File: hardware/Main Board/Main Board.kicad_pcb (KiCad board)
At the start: 2 copper layers, 119 x 56 mm, 32 parts, among them J1 DEC Motor, J2 RA Motor, J3 Battery, J4 Joystick Debug, J5 Joystick Connector, P1 Conn_02x20_Odd_Even, Q1 2N3904, Q2 2N3904, Q3 2N3904, Q4 2N3904, Q5 2N3904, U1 ELEGOO, U2 RA Driver, U3 BuckConverter, U4 BuckConverter

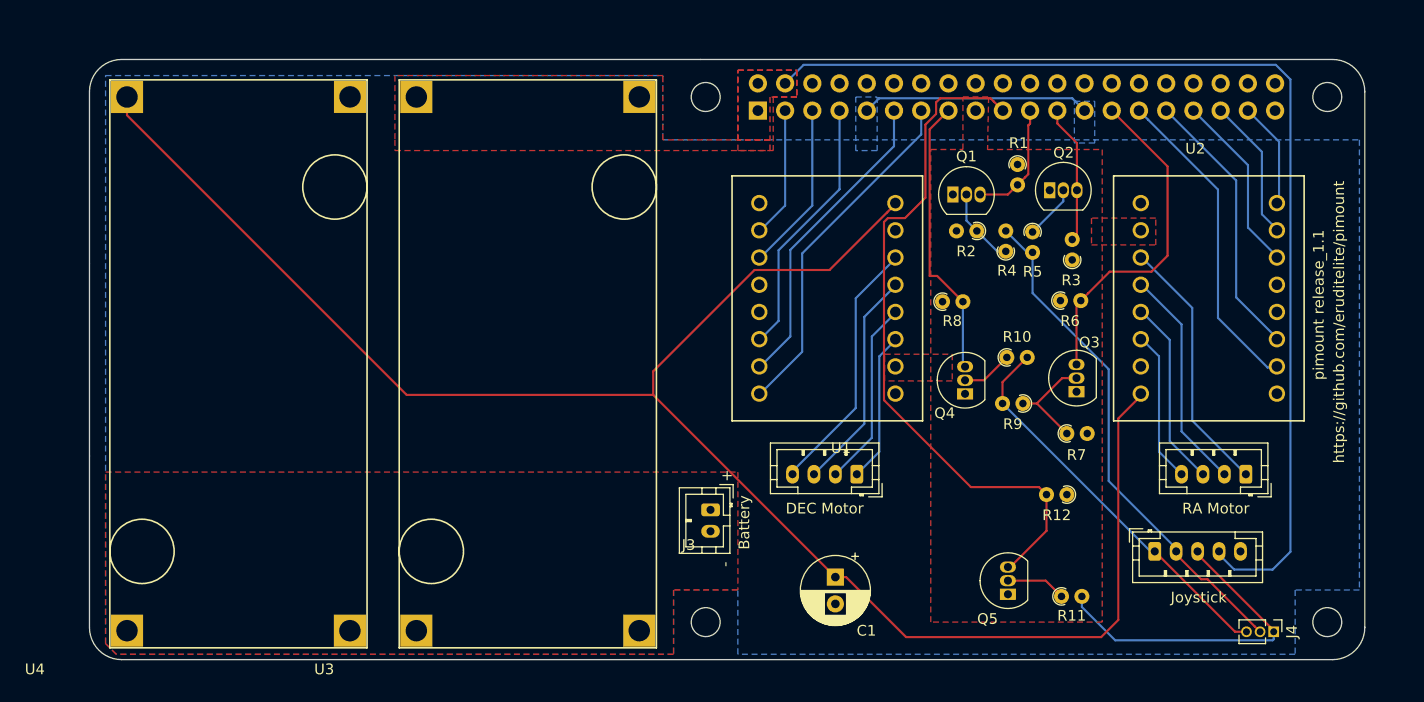
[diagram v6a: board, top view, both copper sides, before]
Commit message: Add a Fan Control Circuit
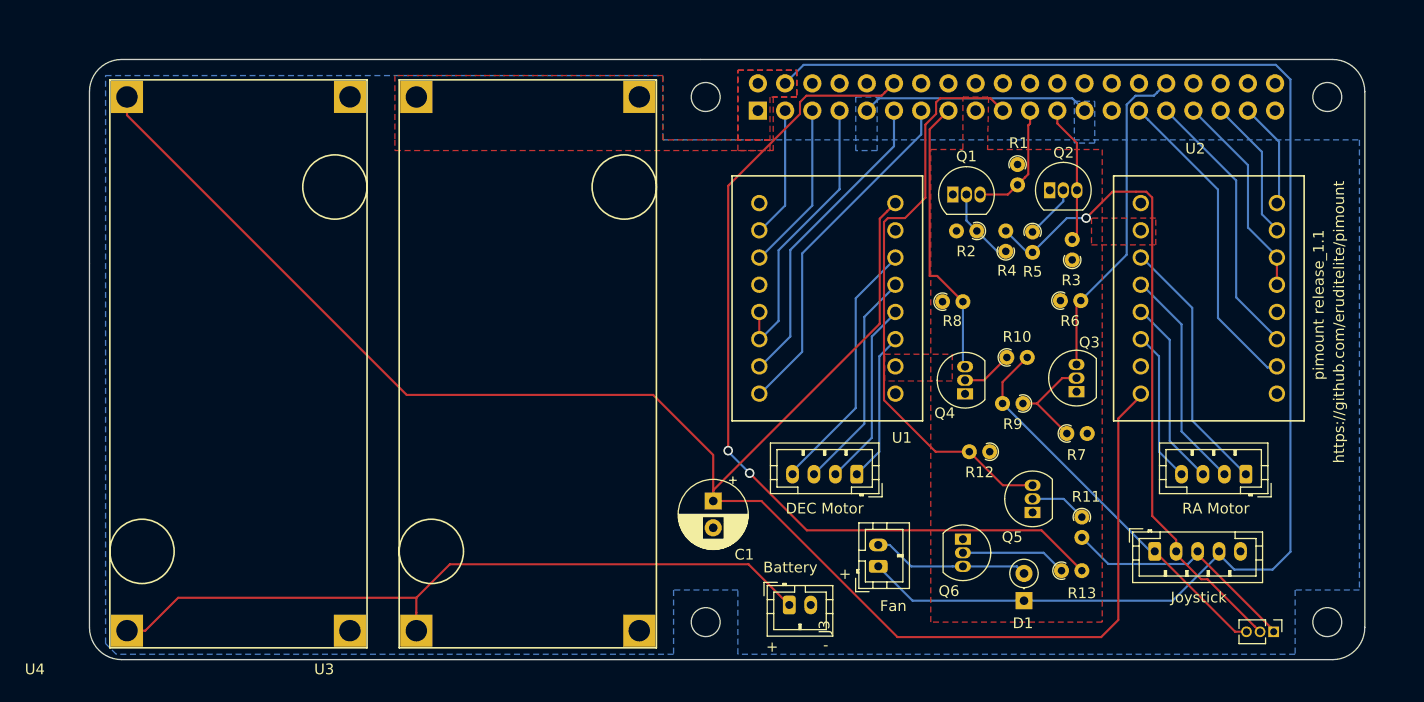
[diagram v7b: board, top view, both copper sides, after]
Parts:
- added D1: 1N4148, Diode_THT:D_DO-35_SOD27_P2.54mm_Vertical_KathodeUp, F.Cu at (229.7, 148.0)
- added J6: Fan, Connector_JST:JST_PH_B2B-PH-K_1x02_P2.00mm_Vertical, F.Cu at (216.1, 144.8)
- added Q6: S8050, Package_TO_SOT_THT:TO-92_Inline, F.Cu at (224.0, 142.3)
- added R13: 1K, Resistor_THT:R_Axial_DIN0204_L3.6mm_D1.6mm_P1.90mm_Vertical, F.Cu at (233.2, 145.2)
- moved C1 13.4 mm to (200.7, 138.7)
- moved J3 11.5 mm to (207.8, 148.4), turned to 0 degrees
- moved R12 8.24 mm to (226.5, 134.1)
- moved Q5 7.97 mm to (230.5, 139.8)
- moved R11 7.64 mm to (235.1, 140.2), turned to 270 degrees
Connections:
- net +6V renamed +10V
- Q3 pad 3: /ID_SD -> /GPIO12(PWM0)
- R6 pad 2: /ID_SD -> /GPIO12(PWM0)
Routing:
- net /GPIO18(GEN1)(PWM0): track 0.00 -> 82.5 mm, vias 0 -> 2
- net Net-(J3-Pad1): track 0.00 -> 69.0 mm
- net +5V: track 100.7 -> 135.6 mm
- net /ID_SD: track 31.7 -> 0.00 mm
- net /GPIO12(PWM0): track 0.00 -> 30.7 mm
- net Net-(D1-Pad2): track 0.00 -> 14.7 mm
- net Net-(J4-Pad2): track 47.9 -> 62.4 mm, vias 0 -> 1
- net /GPIO10(SPI0_MOSI): track 64.8 -> 54.8 mm
- net Net-(Q6-Pad2): track 0.00 -> 9.89 mm
- net Net-(J4-Pad1): track 31.4 -> 22.9 mm
- net +10V: track 168.3 -> 174.4 mm
- net /GPIO4(GCLK): track 24.8 -> 27.4 mm
- net /GPIO13(PWM1): track 17.1 -> 19.7 mm
- removed copper zone on F.Cu, net Net-(J3-Pad1)
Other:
- board text added: "Fan"

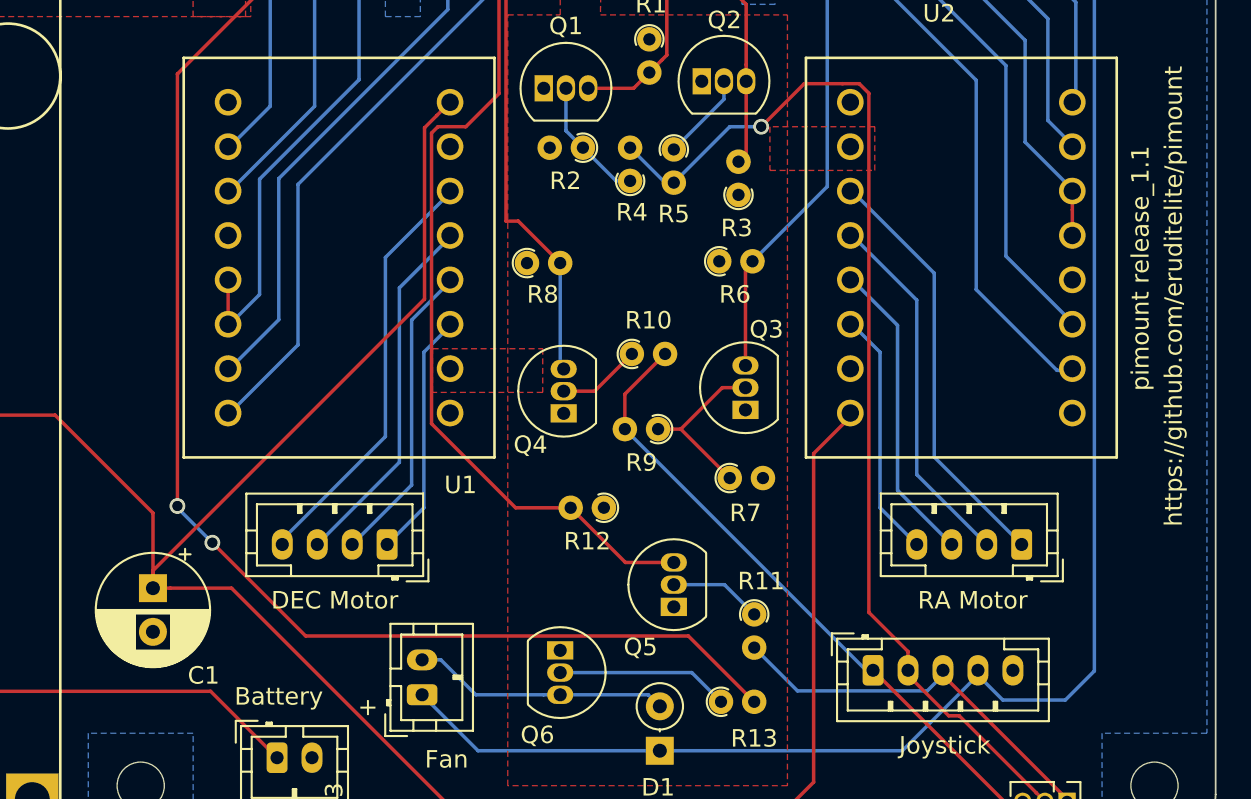
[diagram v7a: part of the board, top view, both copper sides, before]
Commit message: Update the Board Info and Silk Screen to 1.2
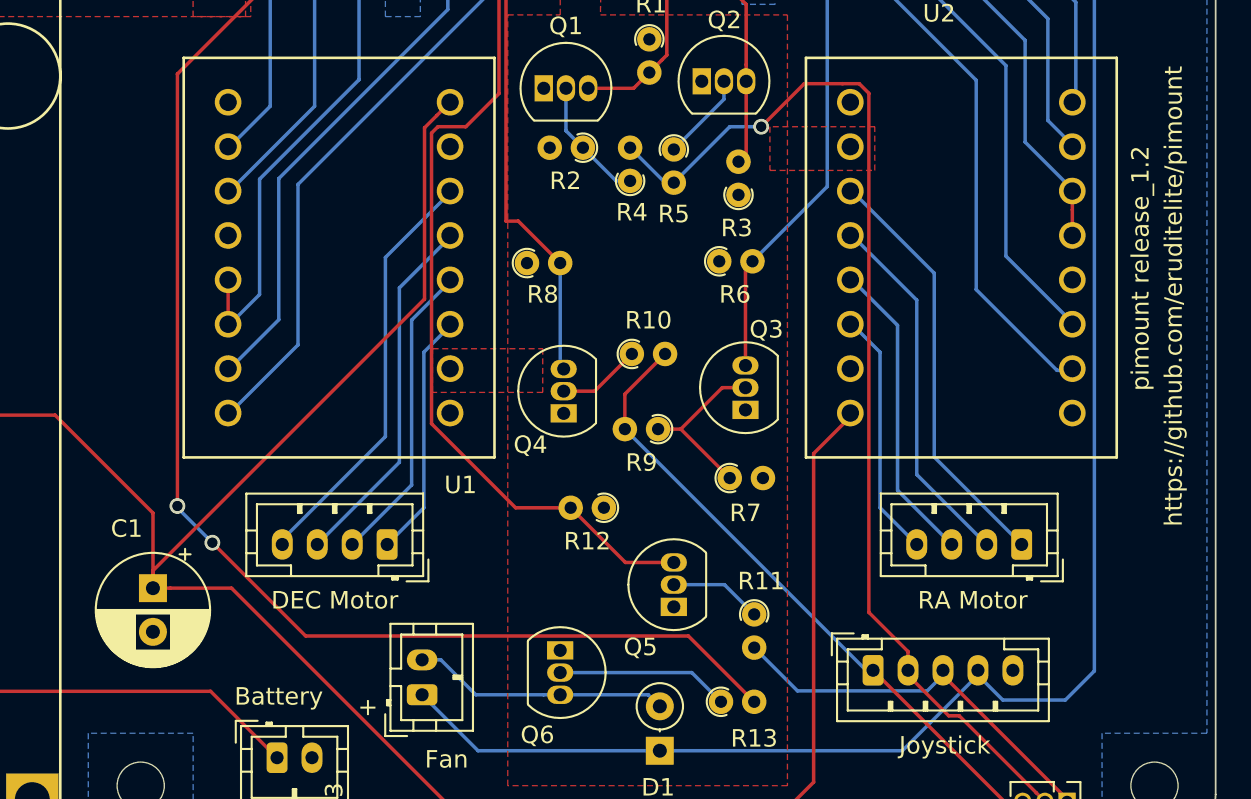
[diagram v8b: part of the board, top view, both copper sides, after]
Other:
- board text added: "pimount release_1.2"
- board text removed: "pimount release_1.1"
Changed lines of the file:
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@@
     (descr "CP, Radial series, Radial, pin pitch=2.50mm, , diameter=6.3mm, Electrolytic Capacitor")
     (tags "CP Radial series Radial pin pitch 2.50mm  diameter 6.3mm Electrolytic Capacitor")
-    (fp_text reference C1 (at 5 -2.9) (layer F.SilkS)
+    (fp_text reference C1 (at -3.4 1.5) (layer F.SilkS)
       (effects (font (size 1 1) (thickness 0.15)))
     )
@@
     (effects (font (size 1 1) (thickness 0.15)))
   )
-  (gr_text "pimount release_1.1" (at 257.2 120.4 90) (layer F.SilkS)
+  (gr_text "pimount release_1.2" (at 257.2 120.4 90) (layer F.SilkS)
     (effects (font (size 1 1) (thickness 0.15)))
   )
@@
   (segment (start 253.5 113.54) (end 251.9 111.94) (width 0.2) (layer B.Cu) (net 28))
   (segment (start 251.9 111.94) (end 251.9 106.12) (width 0.2) (layer B.Cu) (net 28))
-  (segment (start 172.1 128.8) (end 195.1 128.8) (width 0.2) (layer F.Cu) (net 60))
-  (segment (start 146 101) (end 146 102.7) (width 0.2) (layer F.Cu) (net 60))
-  (segment (start 146 102.7) (end 172.1 128.8) (width 0.2) (layer F.Cu) (net 60))
   (segment (start 208.1 135.925) (end 208.1 136.2) (width 0.2) (layer B.Cu) (net 39))
   (segment (start 214 130.025) (end 208.1 135.925) (width 0.2) (layer B.Cu) (net 39))
@@
   (segment (start 249.4 150.9) (end 250.46 150.9) (width 0.2) (layer F.Cu) (net 59))
   (segment (start 241.9 143.4) (end 249.4 150.9) (width 0.2) (layer F.Cu) (net 59))
+  (segment (start 172.1 128.8) (end 195.1 128.8) (width 0.2) (layer F.Cu) (net 60))
+  (segment (start 146 101) (end 146 102.7) (width 0.2) (layer F.Cu) (net 60))
+  (segment (start 146 102.7) (end 172.1 128.8) (width 0.2) (layer F.Cu) (net 60))
   (segment (start 200.7 134.4) (end 200.7 138.7) (width 0.2) (layer F.Cu) (net 60))
   (segment (start 195.1 128.8) (end 200.7 134.4) (width 0.2) (layer F.Cu) (net 60))
